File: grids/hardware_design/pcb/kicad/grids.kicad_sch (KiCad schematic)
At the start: 106 parts

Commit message: change LED/SW and crystal
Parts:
- removed Q1: (no value), symbol grids-eagle-import:CRYSTALHC49UP
- removed SW1: (no value), symbol grids-eagle-import:LP4OA1PBCT
- added Q1: 20MHz, Crystal:Crystal_SMD_2520-4Pin_2.5x2.0mm, symbol Device:Crystal_GND24_Small
- added SW1: SW_MEC_5G_2LED, Supercell 1.3:C&K_D6R, symbol Switch:SW_MEC_5G_2LED
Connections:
- net GND: now also SW1.3 (K), SW1.4 (A)
- net SW_RESET: now also SW1.1
- net at R4.2: now also SW1.2
- net at C2.2, IC1.7 (PB6(XTAL1/TOSC1)): now also Q1.3
- net at C7.2, IC1.8 (PB7(XTAL2/TOSC2)): now also Q1.1
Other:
- moved on the sheet: R4

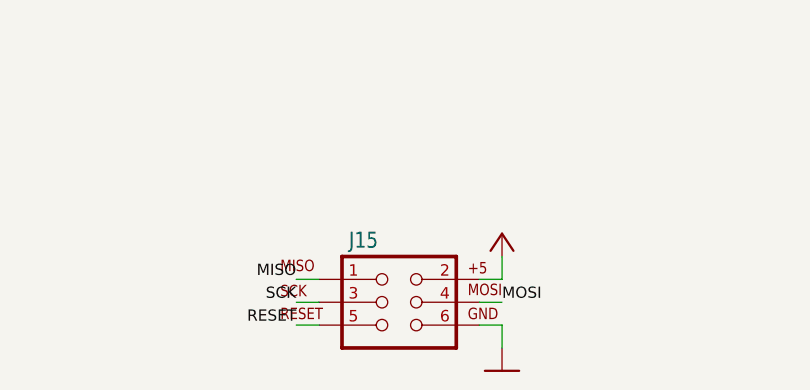
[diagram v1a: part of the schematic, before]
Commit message: add horizontal smd programming header (traces not drawn yet)
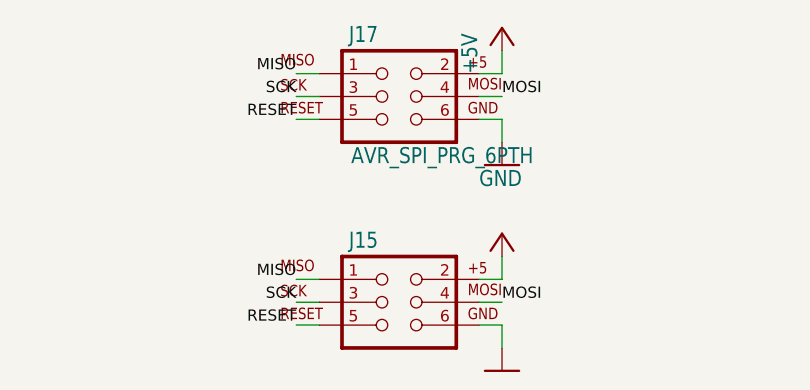
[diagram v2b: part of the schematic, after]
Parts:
- added J17: AVR_SPI_PRG_6PTH, Connector_PinHeader_2.54mm:PinHeader_2x03_P2.54mm_Horizontal_SMD, symbol grids-eagle-import:AVR_SPI_PRG_6PTH
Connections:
- net +5V: now also J17.2
- net GND: now also J17.6
- net MISO: now also J17.1
- net MOSI: now also J17.4
- net RESET: now also J17.5
- net SCK: now also J17.3
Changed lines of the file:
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@@
     (stroke (width 0) (type default) (color 0 0 0 0))
   )
+  (wire (pts (xy 241.3 30.48) (xy 238.76 30.48))
+    (stroke (width 0) (type default) (color 0 0 0 0))
+  )
   (wire (pts (xy 226.06 91.44) (xy 223.52 91.44))
     (stroke (width 0) (type default) (color 0 0 0 0))
@@
     (stroke (width 0) (type default) (color 0 0 0 0))
   )
+  (wire (pts (xy 259.08 33.02) (xy 261.62 33.02))
+    (stroke (width 0) (type default) (color 0 0 0 0))
+  )
   (wire (pts (xy 375.92 109.22) (xy 378.46 109.22))
     (stroke (width 0) (type default) (color 0 0 0 0))
@@
     (stroke (width 0) (type default) (color 0 0 0 0))
   )
+  (wire (pts (xy 261.62 27.94) (xy 261.62 25.4))
+    (stroke (width 0) (type default) (color 0 0 0 0))
+  )
   (wire (pts (xy 226.06 142.24) (xy 223.52 142.24))
     (stroke (width 0) (type default) (color 0 0 0 0))
@@
     (stroke (width 0) (type default) (color 0 0 0 0))
   )
+  (wire (pts (xy 259.08 30.48) (xy 261.62 30.48))
+    (stroke (width 0) (type default) (color 0 0 0 0))
+  )
   (wire (pts (xy 88.9 127) (xy 88.9 134.62))
     (stroke (width 0) (type default) (color 0 0 0 0))
@@
     (stroke (width 0) (type default) (color 0 0 0 0))
   )
+  (wire (pts (xy 241.3 33.02) (xy 238.76 33.02))
+    (stroke (width 0) (type default) (color 0 0 0 0))
+  )
   (wire (pts (xy 45.72 48.26) (xy 55.88 48.26))
     (stroke (width 0) (type default) (color 0 0 0 0))
@@
     (stroke (width 0) (type default) (color 0 0 0 0))
   )
+  (wire (pts (xy 241.3 27.94) (xy 238.76 27.94))
+    (stroke (width 0) (type default) (color 0 0 0 0))
+  )
   (wire (pts (xy 200.66 96.52) (xy 200.66 99.06))
     (stroke (width 0) (type default) (color 0 0 0 0))
@@
     (stroke (width 0) (type default) (color 0 0 0 0))
   )
+  (wire (pts (xy 261.62 33.02) (xy 261.62 35.56))
+    (stroke (width 0) (type default) (color 0 0 0 0))
+  )
   (wire (pts (xy 320.04 60.96) (xy 332.74 60.96))
     (stroke (width 0) (type default) (color 0 0 0 0))
@@
     (stroke (width 0) (type default) (color 0 0 0 0))
   )
+  (wire (pts (xy 259.08 27.94) (xy 261.62 27.94))
+    (stroke (width 0) (type default) (color 0 0 0 0))
+  )
   (wire (pts (xy 322.58 236.22) (xy 322.58 233.68))
     (stroke (width 0) (type default) (color 0 0 0 0))
@@
     (effects (font (size 1.2446 1.2446)) (justify left bottom))
   )
+  (label "RESET" (at 238.76 33.02 180)
+    (effects (font (size 1.2446 1.2446)) (justify right bottom))
+  )
   (label "IN_RESET" (at 276.86 119.38 0)
     (effects (font (size 1.2446 1.2446)) (justify left bottom))
@@
     (effects (font (size 1.2446 1.2446)) (justify left bottom))
   )
+  (label "SCK" (at 238.76 30.48 180)
+    (effects (font (size 1.2446 1.2446)) (justify right bottom))
+  )
   (label "REF_-5" (at 332.74 233.68 0)
     (effects (font (size 1.2446 1.2446)) (justify left bottom))
@@
     (effects (font (size 1.2446 1.2446)) (justify left bottom))
   )
+  (label "MOSI" (at 261.62 30.48 0)
+    (effects (font (size 1.2446 1.2446)) (justify left bottom))
+  )
   (label "REF_-5" (at 53.34 55.88 270)
     (effects (font (size 1.2446 1.2446)) (justify right bottom))
   )
+  (label "MISO" (at 238.76 27.94 180)
+    (effects (font (size 1.2446 1.2446)) (justify right bottom))
+  )
   (label "TEMPO" (at 276.86 106.68 0)
     (effects (font (size 1.2446 1.2446)) (justify left bottom))
@@
     (pin "2")
   )
+  (symbol (lib_id "grids-eagle-import:GND") (at 261.62 38.1 0) (unit 1)
+    (in_bom yes) (on_board yes)
+    (property "Reference" "#GND0102" (id 0) (at 261.62 38.1 0)
+      (effects (font (size 1.27 1.27)) hide)
+    )
+    (property "Value" "GND" (id 1) (at 259.08 40.64 0)
+      (effects (font (size 1.778 1.5113)) (justify left bottom))
+    )
+    (property "Footprint" "grids:" (id 2) (at 261.62 38.1 0)
+      (effects (font (size 1.27 1.27)) hide)
+    )
+    (property "Datasheet" "" (id 3) (at 261.62 38.1 0)
+      (effects (font (size 1.27 1.27)) hide)
+    )
+    (pin "1")
+  )
   (symbol (lib_id "grids-eagle-import:TL072D") (at 78.74 58.42 0) (mirror x) (unit 1)
     (in_bom yes) (on_board yes)
@@
     (pin "2")
   )
+  (symbol (lib_id "grids-eagle-import:AVR_SPI_PRG_6PTH") (at 248.92 30.48 0) (unit 1)
+    (in_bom yes) (on_board yes)
+    (property "Reference" "J17" (id 0) (at 244.602 24.638 0)
+      (effects (font (size 1.778 1.5113)) (justify left bottom))
+    )
+    (property "Value" "AVR_SPI_PRG_6PTH" (id 1) (at 244.856 38.1 0)
+      (effects (font (size 1.778 1.5113)) (justify left bottom))
+    )
+    (property "Footprint" "Connector_PinHeader_2.54mm:PinHeader_2x03_P2.54mm_Horizontal_SMD" (id 2) (at 248.92 30.48 0)
+      (effects (font (size 1.27 1.27)) hide)
+    )
+    (property "Datasheet" "" (id 3) (at 248.92 30.48 0)
+      (effects (font (size 1.27 1.27)) hide)
+    )
+    (pin "1")
+    (pin "2")
+    (pin "3")
+    (pin "4")
+    (pin "5")
+    (pin "6")
+  )
   (symbol (lib_id "grids-eagle-import:POT_USVERTICAL_PS") (at 106.68 43.18 0) (unit 1)
     (in_bom yes) (on_board yes)
@@
     (pin "1")
   )
+  (symbol (lib_id "grids-eagle-import:+5V") (at 261.62 22.86 0) (unit 1)
+    (in_bom yes) (on_board yes)
+    (property "Reference" "#P+0101" (id 0) (at 261.62 22.86 0)
+      (effects (font (size 1.27 1.27)) hide)
+    )
+    (property "Value" "+5V" (id 1) (at 259.08 27.94 90)
+      (effects (font (size 1.778 1.5113)) (justify left bottom))
+    )
+    (property "Footprint" "grids:" (id 2) (at 261.62 22.86 0)
+      (effects (font (size 1.27 1.27)) hide)
+    )
+    (property "Datasheet" "" (id 3) (at 261.62 22.86 0)
+      (effects (font (size 1.27 1.27)) hide)
+    )
+    (pin "1")
+  )
   (symbol (lib_id "grids-eagle-import:GND") (at 106.68 101.6 0) (unit 1)
     (in_bom yes) (on_board yes)
@@
       (reference "#GND0101") (unit 1) (value "GND") (footprint "grids:")
     )
+    (path "/541f42bd-8c77-4a8c-ba32-16c1eee8da38"
+      (reference "#GND0102") (unit 1) (value "GND") (footprint "grids:")
+    )
     (path "/b300c688-3f12-4d55-ab97-ba780d08af7c"
       (reference "#P+01") (unit 1) (value "+5V") (footprint "grids:")
@@
       (reference "#P+020") (unit 1) (value "VCC") (footprint "grids:")
     )
+    (path "/e63adc6a-248d-43a9-b07a-a624e39cc902"
+      (reference "#P+0101") (unit 1) (value "+5V") (footprint "grids:")
+    )
     (path "/ffc07d96-46ce-47a5-91db-bbf61d82b738"
       (reference "#SUPPLY01") (unit 1) (value "VEE") (footprint "grids:")
@@
       (reference "J16") (unit 1) (value "M05X2PTH") (footprint "grids:AVR_ICSP")
     )
+    (path "/c4806849-a52f-4044-a9a3-89c85746da09"
+      (reference "J17") (unit 1) (value "AVR_SPI_PRG_6PTH") (footprint "Connector_PinHeader_2.54mm:PinHeader_2x03_P2.54mm_Horizontal_SMD")
+    )
     (path "/a7dbf5d9-6187-4d91-a8c4-2aa58ed2804f"

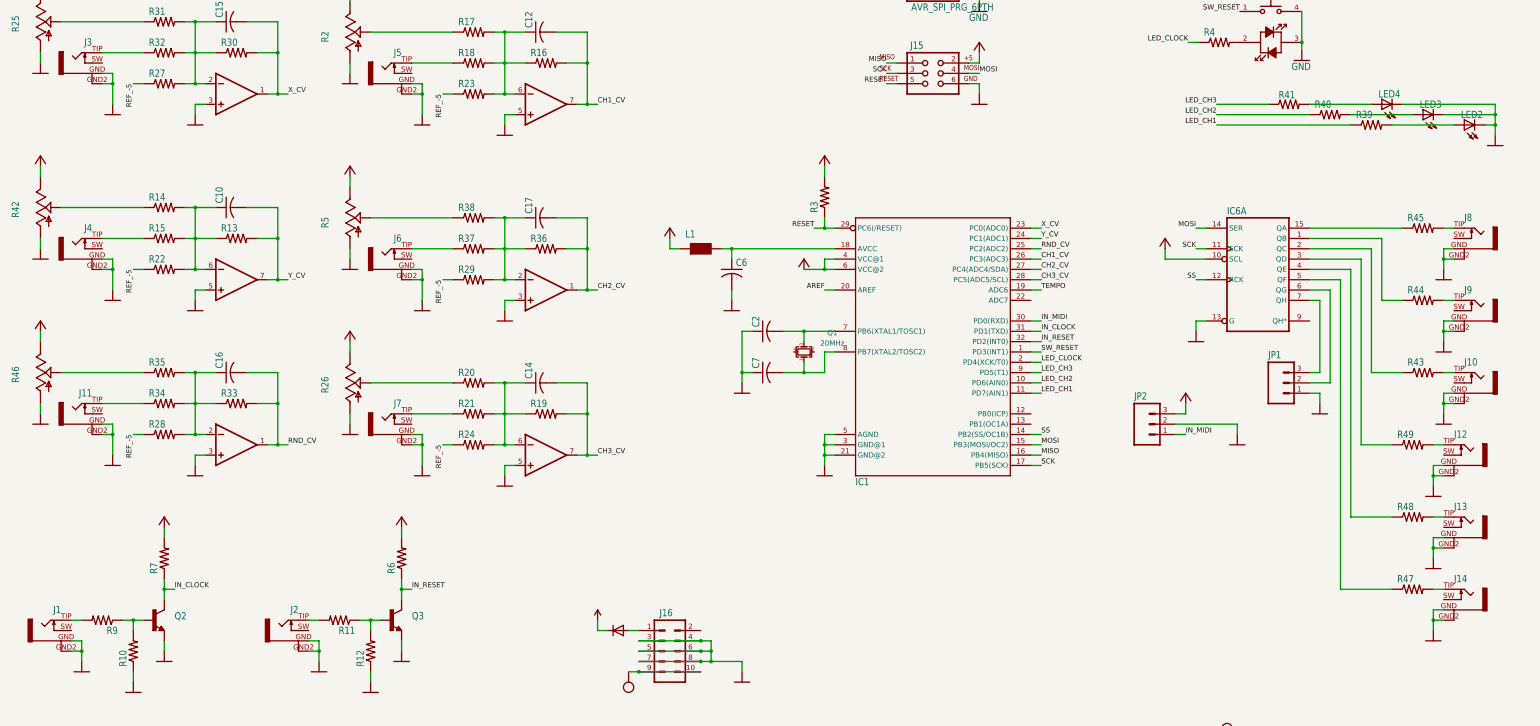
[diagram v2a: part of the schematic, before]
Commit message: changed jacks
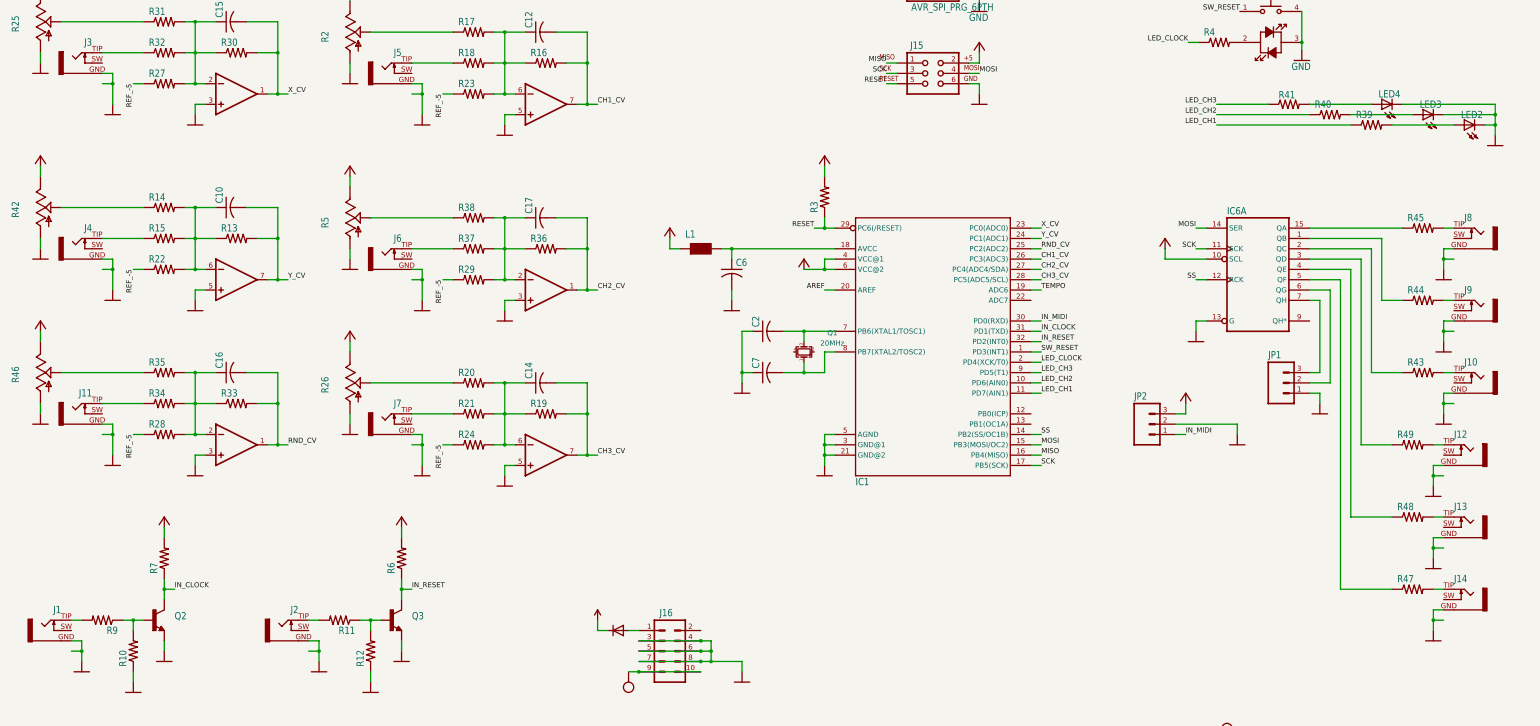
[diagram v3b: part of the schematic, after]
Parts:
- J1, J10, J11, J12, J13, J14, J3, J4, J5, J6, J7, J8, J9: footprint (none) -> marbles:WQP_PJ_301M6
- J2: value (none) -> PJ301WQP; footprint (none) -> marbles:WQP_PJ_301M6
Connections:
- net GND: no longer J1.GND2 (4), J10.GND2 (4), J11.GND2 (4), J12.GND2 (4), J13.GND2 (4), J14.GND2 (4), J2.GND2 (4), J3.GND2 (4), J4.GND2 (4), J5.GND2 (4), J6.GND2 (4), J7.GND2 (4), J8.GND2 (4), J9.GND2 (4)
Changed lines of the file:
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@@
     (pin "2")
   )
-  (symbol (lib_id "grids-eagle-import:PJ301WQP") (at 91.44 190.5 0) (mirror y) (unit 1)
+  (symbol (lib_name "PJ301WQP_12") (lib_id "grids-eagle-import:PJ301WQP") (at 91.44 190.5 0) (mirror y) (unit 1)
     (in_bom yes) (on_board yes)
     (property "Reference" "J2" (id 0) (at 93.98 186.436 0)
       (effects (font (size 1.778 1.5113)) (justify left bottom))
     )
-    (property "Value" "" (id 1) (at 91.44 190.5 0)
-      (effects (font (size 1.27 1.27)) hide)
-    )
-    (property "Footprint" "" (id 2) (at 91.44 190.5 0)
+    (property "Value" "PJ301WQP" (id 1) (at 91.44 190.5 0)
+      (effects (font (size 1.27 1.27)) hide)
+    )
+    (property "Footprint" "marbles:WQP_PJ_301M6" (id 2) (at 91.44 190.5 0)
       (effects (font (size 1.27 1.27)) hide)
     )
@@
     )
     (pin "GND")
-    (pin "GND2")
     (pin "SW")
     (pin "TIP")
@@
     (pin "1")
   )
-  (symbol (lib_id "grids-eagle-import:PJ301WQP") (at 383.54 129.54 0) (unit 1)
+  (symbol (lib_name "PJ301WQP_10") (lib_id "grids-eagle-import:PJ301WQP") (at 383.54 129.54 0) (unit 1)
     (in_bom yes) (on_board yes)
     (property "Reference" "J10" (id 0) (at 381 125.476 0)
@@
       (effects (font (size 1.27 1.27)) hide)
     )
-    (property "Footprint" "" (id 2) (at 383.54 129.54 0)
+    (property "Footprint" "marbles:WQP_PJ_301M6" (id 2) (at 383.54 129.54 0)
       (effects (font (size 1.27 1.27)) hide)
     )
@@
     )
     (pin "GND")
-    (pin "GND2")
     (pin "SW")
     (pin "TIP")
@@
     (pin "1")
   )
-  (symbol (lib_id "grids-eagle-import:PJ301WQP") (at 381 147.32 0) (unit 1)
+  (symbol (lib_name "PJ301WQP_9") (lib_id "grids-eagle-import:PJ301WQP") (at 381 147.32 0) (unit 1)
     (in_bom yes) (on_board yes)
     (property "Reference" "J12" (id 0) (at 378.46 143.256 0)
@@
       (effects (font (size 1.27 1.27)) hide)
     )
-    (property "Footprint" "" (id 2) (at 381 147.32 0)
+    (property "Footprint" "marbles:WQP_PJ_301M6" (id 2) (at 381 147.32 0)
       (effects (font (size 1.27 1.27)) hide)
     )
@@
     )
     (pin "GND")
-    (pin "GND2")
     (pin "SW")
     (pin "TIP")
   )
-  (symbol (lib_id "grids-eagle-import:PJ301WQP") (at 40.64 50.8 0) (mirror y) (unit 1)
+  (symbol (lib_name "PJ301WQP_3") (lib_id "grids-eagle-import:PJ301WQP") (at 40.64 50.8 0) (mirror y) (unit 1)
     (in_bom yes) (on_board yes)
     (property "Reference" "J3" (id 0) (at 43.18 46.736 0)
@@
       (effects (font (size 1.27 1.27)) hide)
     )
-    (property "Footprint" "" (id 2) (at 40.64 50.8 0)
+    (property "Footprint" "marbles:WQP_PJ_301M6" (id 2) (at 40.64 50.8 0)
       (effects (font (size 1.27 1.27)) hide)
     )
@@
     )
     (pin "GND")
-    (pin "GND2")
     (pin "SW")
     (pin "TIP")
@@
       (effects (font (size 1.27 1.27)) hide)
     )
-    (property "Footprint" "" (id 2) (at 381 182.88 0)
+    (property "Footprint" "marbles:WQP_PJ_301M6" (id 2) (at 381 182.88 0)
       (effects (font (size 1.27 1.27)) hide)
     )
@@
     )
     (pin "GND")
-    (pin "GND2")
     (pin "SW")
     (pin "TIP")
@@
     (pin "2")
   )
-  (symbol (lib_id "grids-eagle-import:PJ301WQP") (at 33.02 190.5 0) (mirror y) (unit 1)
+  (symbol (lib_name "PJ301WQP_11") (lib_id "grids-eagle-import:PJ301WQP") (at 33.02 190.5 0) (mirror y) (unit 1)
     (in_bom yes) (on_board yes)
     (property "Reference" "J1" (id 0) (at 35.56 186.436 0)
@@
       (effects (font (size 1.27 1.27)) hide)
     )
-    (property "Footprint" "" (id 2) (at 33.02 190.5 0)
+    (property "Footprint" "marbles:WQP_PJ_301M6" (id 2) (at 33.02 190.5 0)
       (effects (font (size 1.27 1.27)) hide)
     )
@@
     )
     (pin "GND")
-    (pin "GND2")
     (pin "SW")
     (pin "TIP")
@@
     (pin "1")
   )
-  (symbol (lib_id "grids-eagle-import:PJ301WQP") (at 116.84 139.7 0) (mirror y) (unit 1)
+  (symbol (lib_name "PJ301WQP_1") (lib_id "grids-eagle-import:PJ301WQP") (at 116.84 139.7 0) (mirror y) (unit 1)
     (in_bom yes) (on_board yes)
     (property "Reference" "J7" (id 0) (at 119.38 135.636 0)
@@
       (effects (font (size 1.27 1.27)) hide)
     )
-    (property "Footprint" "" (id 2) (at 116.84 139.7 0)
+    (property "Footprint" "marbles:WQP_PJ_301M6" (id 2) (at 116.84 139.7 0)
       (effects (font (size 1.27 1.27)) hide)
     )
@@
     )
     (pin "GND")
-    (pin "GND2")
     (pin "SW")
     (pin "TIP")
@@
     (pin "8")
   )
-  (symbol (lib_id "grids-eagle-import:PJ301WQP") (at 40.64 137.16 0) (mirror y) (unit 1)
+  (symbol (lib_name "PJ301WQP_6") (lib_id "grids-eagle-import:PJ301WQP") (at 40.64 137.16 0) (mirror y) (unit 1)
     (in_bom yes) (on_board yes)
     (property "Reference" "J11" (id 0) (at 43.18 133.096 0)
@@
       (effects (font (size 1.27 1.27)) hide)
     )
-    (property "Footprint" "" (id 2) (at 40.64 137.16 0)
+    (property "Footprint" "marbles:WQP_PJ_301M6" (id 2) (at 40.64 137.16 0)
       (effects (font (size 1.27 1.27)) hide)
     )
@@
     )
     (pin "GND")
-    (pin "GND2")
     (pin "SW")
     (pin "TIP")
@@
     (pin "6")
   )
-  (symbol (lib_id "grids-eagle-import:PJ301WQP") (at 383.54 111.76 0) (unit 1)
+  (symbol (lib_name "PJ301WQP_7") (lib_id "grids-eagle-import:PJ301WQP") (at 383.54 111.76 0) (unit 1)
     (in_bom yes) (on_board yes)
     (property "Reference" "J9" (id 0) (at 381 107.696 0)
@@
       (effects (font (size 1.27 1.27)) hide)
     )
-    (property "Footprint" "" (id 2) (at 383.54 111.76 0)
+    (property "Footprint" "marbles:WQP_PJ_301M6" (id 2) (at 383.54 111.76 0)
       (effects (font (size 1.27 1.27)) hide)
     )
@@
     )
     (pin "GND")
-    (pin "GND2")
     (pin "SW")
     (pin "TIP")
@@
     (pin "2")
   )
-  (symbol (lib_id "grids-eagle-import:PJ301WQP") (at 116.84 53.34 0) (mirror y) (unit 1)
+  (symbol (lib_name "PJ301WQP_4") (lib_id "grids-eagle-import:PJ301WQP") (at 116.84 53.34 0) (mirror y) (unit 1)
     (in_bom yes) (on_board yes)
     (property "Reference" "J5" (id 0) (at 119.38 49.276 0)
@@
       (effects (font (size 1.27 1.27)) hide)
     )
-    (property "Footprint" "" (id 2) (at 116.84 53.34 0)
+    (property "Footprint" "marbles:WQP_PJ_301M6" (id 2) (at 116.84 53.34 0)
       (effects (font (size 1.27 1.27)) hide)
     )
@@
     )
     (pin "GND")
-    (pin "GND2")
     (pin "SW")
     (pin "TIP")
@@
     (pin "1")
   )
-  (symbol (lib_id "grids-eagle-import:PJ301WQP") (at 383.54 93.98 0) (unit 1)
+  (symbol (lib_name "PJ301WQP_8") (lib_id "grids-eagle-import:PJ301WQP") (at 383.54 93.98 0) (unit 1)
     (in_bom yes) (on_board yes)
     (property "Reference" "J8" (id 0) (at 381 89.916 0)
@@
       (effects (font (size 1.27 1.27)) hide)
     )
-    (property "Footprint" "" (id 2) (at 383.54 93.98 0)
+    (property "Footprint" "marbles:WQP_PJ_301M6" (id 2) (at 383.54 93.98 0)
       (effects (font (size 1.27 1.27)) hide)
     )
@@
     )
     (pin "GND")
-    (pin "GND2")
     (pin "SW")
     (pin "TIP")
@@
     (pin "1")
   )
-  (symbol (lib_id "grids-eagle-import:PJ301WQP") (at 116.84 99.06 0) (mirror y) (unit 1)
+  (symbol (lib_name "PJ301WQP_2") (lib_id "grids-eagle-import:PJ301WQP") (at 116.84 99.06 0) (mirror y) (unit 1)
     (in_bom yes) (on_board yes)
     (property "Reference" "J6" (id 0) (at 119.38 94.996 0)
@@
       (effects (font (size 1.27 1.27)) hide)
     )
-    (property "Footprint" "" (id 2) (at 116.84 99.06 0)
+    (property "Footprint" "marbles:WQP_PJ_301M6" (id 2) (at 116.84 99.06 0)
       (effects (font (size 1.27 1.27)) hide)
     )
@@
     )
     (pin "GND")
-    (pin "GND2")
     (pin "SW")
     (pin "TIP")
@@
     (pin "P$3")
   )
-  (symbol (lib_id "grids-eagle-import:PJ301WQP") (at 40.64 96.52 0) (mirror y) (unit 1)
+  (symbol (lib_name "PJ301WQP_5") (lib_id "grids-eagle-import:PJ301WQP") (at 40.64 96.52 0) (mirror y) (unit 1)
     (in_bom yes) (on_board yes)
     (property "Reference" "J4" (id 0) (at 43.18 92.456 0)
@@
       (effects (font (size 1.27 1.27)) hide)
     )
-    (property "Footprint" "" (id 2) (at 40.64 96.52 0)
+    (property "Footprint" "marbles:WQP_PJ_301M6" (id 2) (at 40.64 96.52 0)
       (effects (font (size 1.27 1.27)) hide)
     )
@@
     )
     (pin "GND")
-    (pin "GND2")
     (pin "SW")
     (pin "TIP")
   )
-  (symbol (lib_id "grids-eagle-import:PJ301WQP") (at 381 165.1 0) (unit 1)
+  (symbol (lib_name "PJ301WQP_13") (lib_id "grids-eagle-import:PJ301WQP") (at 381 165.1 0) (unit 1)
     (in_bom yes) (on_board yes)
     (property "Reference" "J13" (id 0) (at 378.46 161.036 0)
@@
       (effects (font (size 1.27 1.27)) hide)
     )
-    (property "Footprint" "" (id 2) (at 381 165.1 0)
+    (property "Footprint" "marbles:WQP_PJ_301M6" (id 2) (at 381 165.1 0)
       (effects (font (size 1.27 1.27)) hide)
     )
@@
     )
     (pin "GND")
-    (pin "GND2")
     (pin "SW")
     (pin "TIP")
